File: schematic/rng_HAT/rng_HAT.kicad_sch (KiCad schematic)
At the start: 24 parts, among them J1 RPi_GPIO, Q1 2N3904, Q2 2N3904, Q3 2N3904, Q4 BC107, Q5 2N3904, U3 STM32F103C8Tx

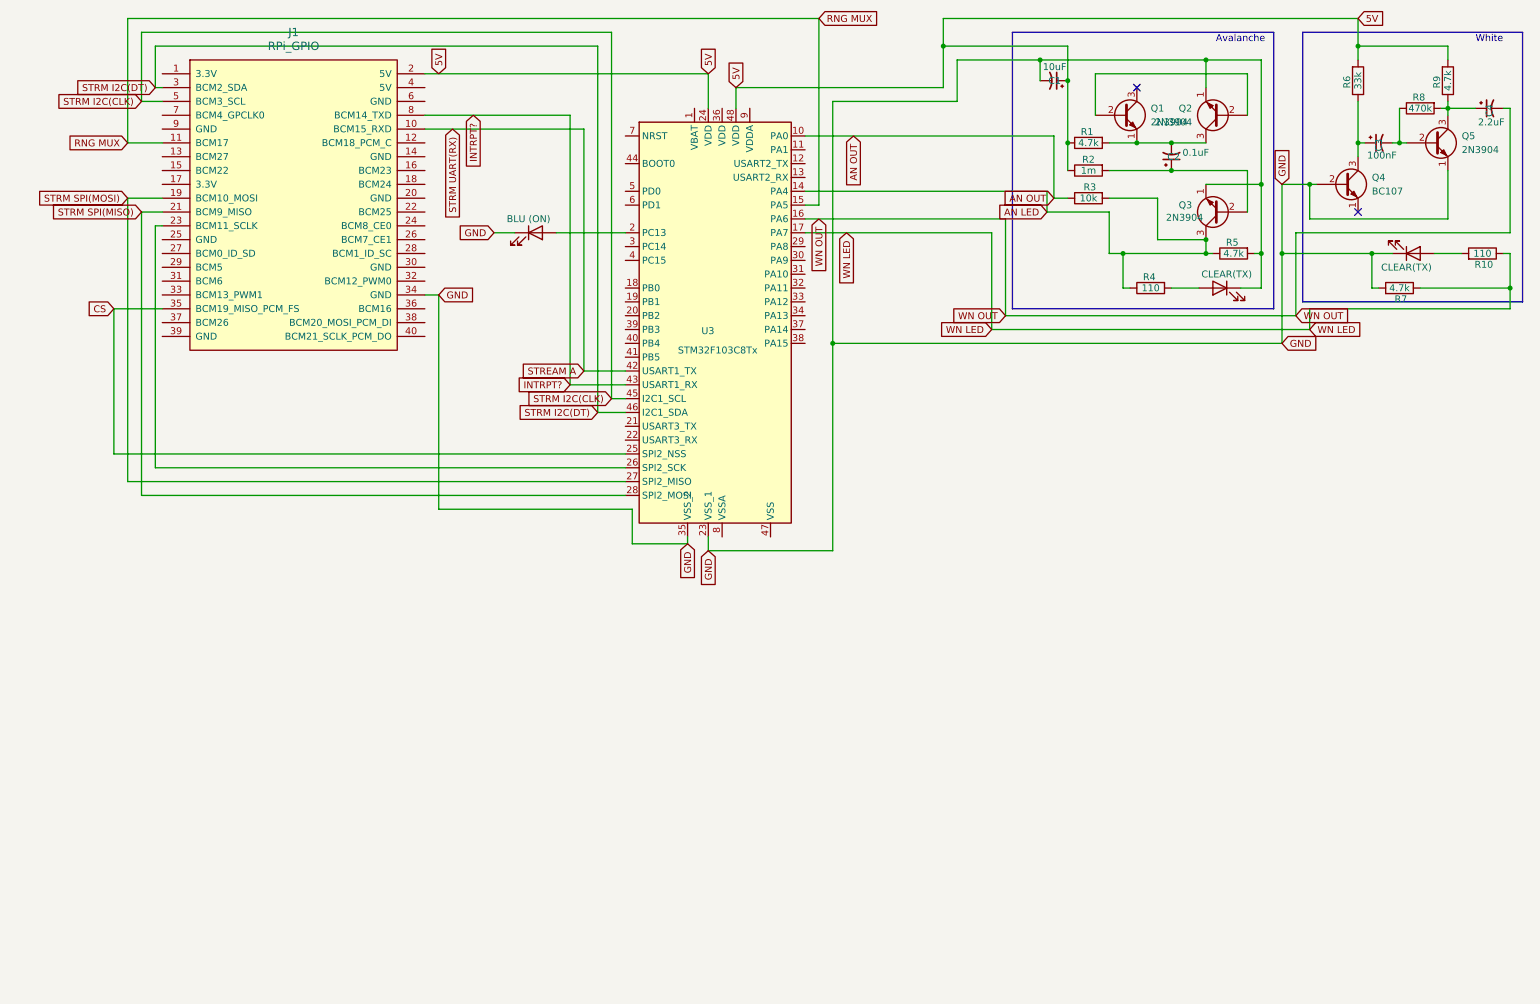
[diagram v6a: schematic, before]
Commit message: different layer for serial lines and analog lines?
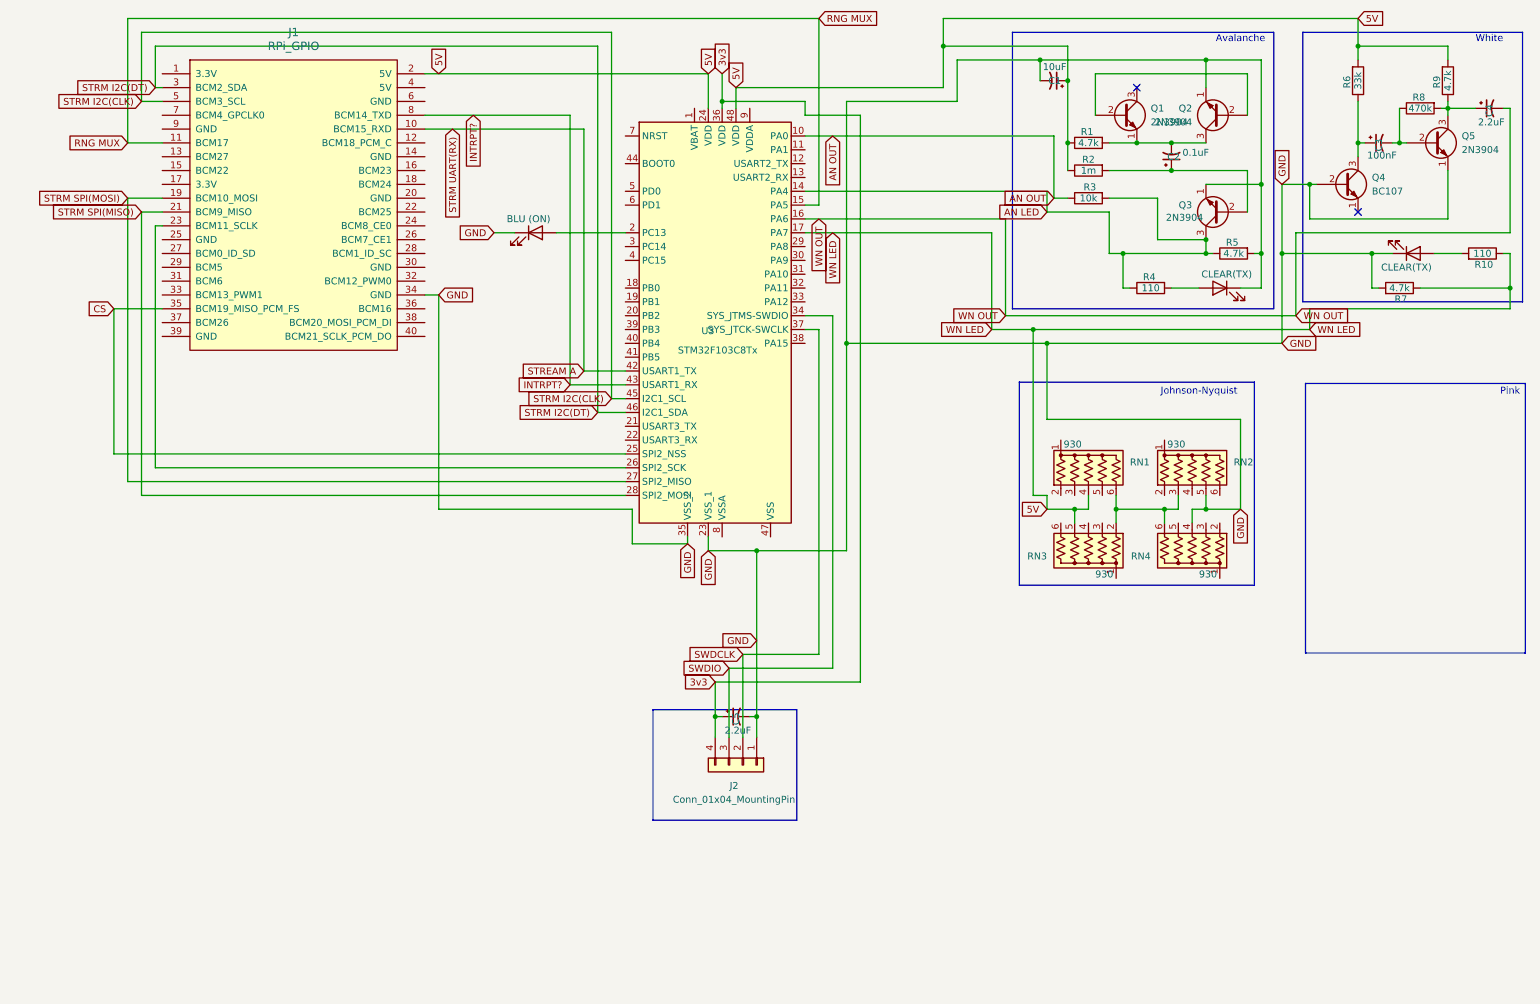
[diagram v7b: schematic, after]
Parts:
- added C5: 2.2uF, Capacitor_SMD:CP_Elec_3x5.3, symbol Device:C_Polarized_Small_US
- added J2: Conn_01x04_MountingPin, Connector_PinHeader_1.00mm:PinHeader_1x04_P1.00mm_Horizontal, symbol Connector_Generic_MountingPin:Conn_01x04_MountingPin
- added RN1, RN2, RN3, RN4: 930, Resistor_THT:R_Array_SIP6, symbol Device:R_Network05_US
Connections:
- net WN LED is gone; now on net 5V: R10.1, R7.1, U3.17 (PA7)
- net 5V: now also RN1.4 (R3), RN3.5 (R4)
- net GND: now also C5.2, J2.1 (GND), RN2.5 (R4), RN4.4 (R3)
- net SWDIO: now reaches U3.34 (PA13)
- net SWDIO: now also J2.3 (SWDIO)
- net 3v3: now reaches U3.36 (VDD)
- net 3v3: now also C5.1, J2.4 (3v3)
- net SWDCLK: now reaches U3.37 (PA14)
- net SWDCLK: now also J2.2 (SWDCLK)
- new net: RN1.6 (R5), RN2.3 (R2), RN3.2 (R1), RN4.6 (R5)
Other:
- note added: "Johnson-Nyquist"
- note added: "Pink"

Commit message: very broken! reverting and redoing
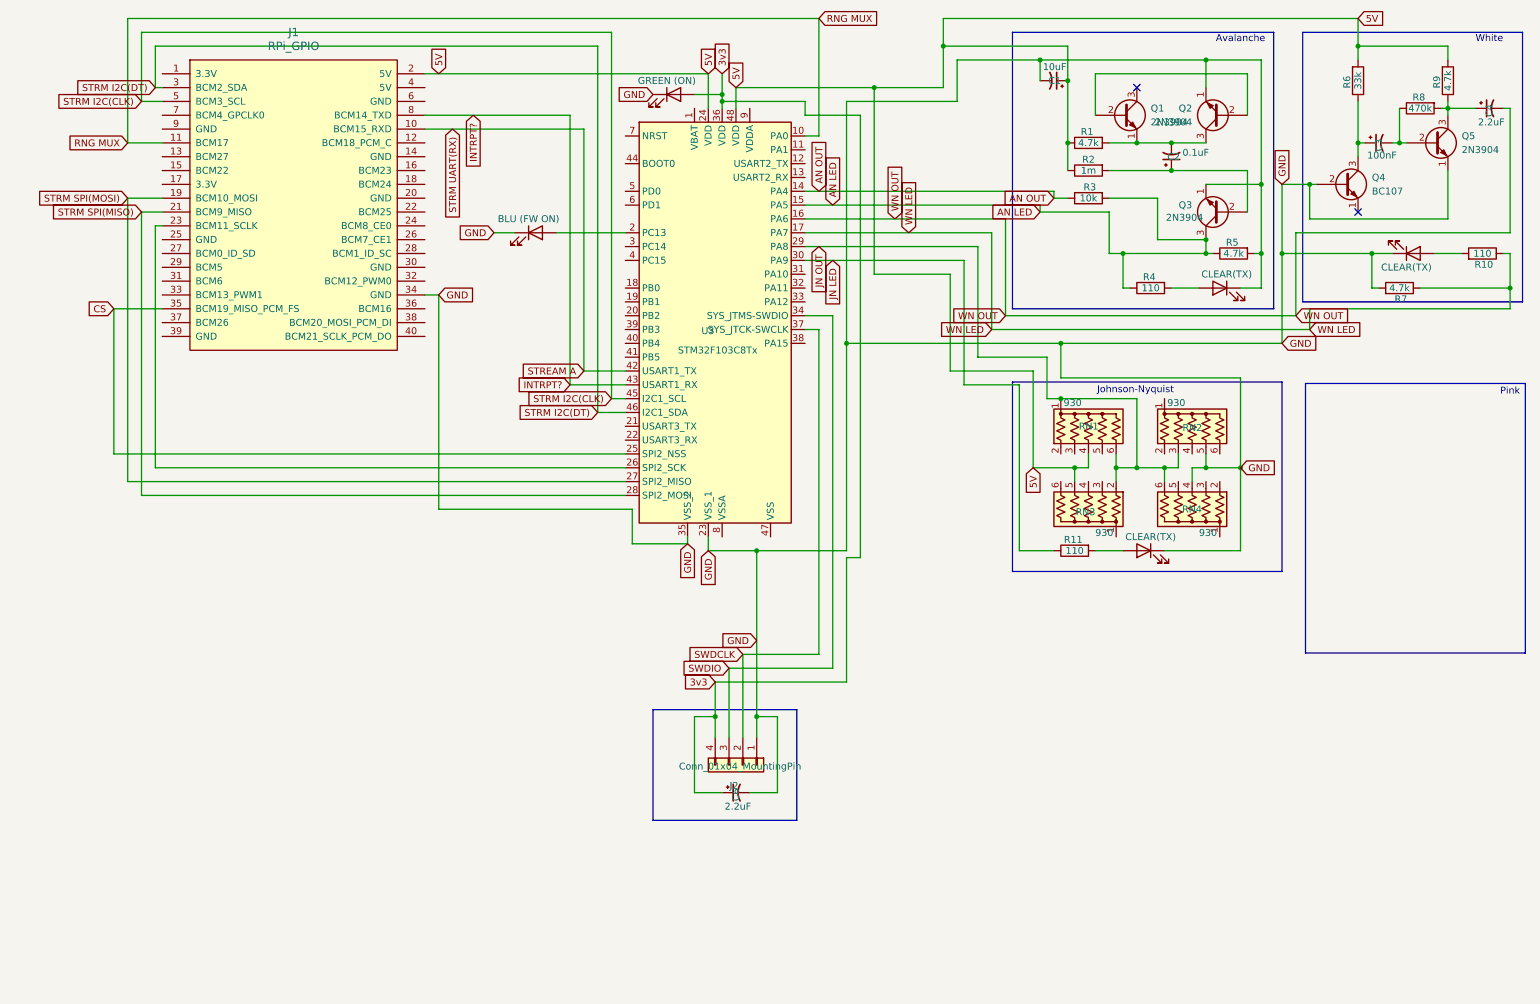
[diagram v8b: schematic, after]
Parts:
- removed C5: 2.2uF, Capacitor_SMD:CP_Elec_3x5.3, symbol Device:C_Polarized_Small_US
- added C6: 2.2uF, Capacitor_SMD:CP_Elec_3x5.3, symbol Device:C_Polarized_Small_US
- added D4: GREEN (ON), LED_SMD:LED_0201_0603Metric, symbol Device:LED
- added D5: CLEAR(TX), LED_SMD:LED_0201_0603Metric, symbol Device:LED
- added R11: 110, Resistor_SMD:R_0201_0603Metric, symbol Device:R
- D1: value BLU (ON) -> BLU (FW ON)
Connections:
- net 3v3: now also C6.1, D4.2 (A)
- net 5V: no longer R10.1, R7.1, U3.17 (PA7)
- net AN LED: now also U3.15 (PA5); no longer U3.14 (PA4)
- net AN OUT: now also U3.14 (PA4); no longer U3.10 (PA0)
- net GND: now also C6.2, D4.1 (K), D5.1 (K)
- net RNG MUX: now also U3.10 (PA0); no longer U3.15 (PA5)
- net JN OUT: now reaches RN1.6 (R5), RN2.3 (R2), RN3.2 (R1), RN4.6 (R5)
- net JN OUT: now also RN1.1 (common), U3.29 (PA8)
- net JN LED: now reaches U3.30 (PA9)
- net JN LED: now also R11.1
- new net: D5.2 (A), R11.2
- new net WN LED: R10.1, R7.1, U3.17 (PA7)
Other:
- moved on the sheet: RN1, RN2, RN3, RN4
